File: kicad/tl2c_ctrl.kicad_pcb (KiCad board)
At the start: 4 copper layers, 38.1 x 66 mm, 65 parts, among them IC101 ATTINY20-X, P101 12VDC, P102 I2C Master, P103 Spare, P104 ISP Header, P105 LED_DRIVER, P301 PIR13, Q301 IRLML2502, Q302 IRLML2502, Q303 IRLML2502, SW101 TL3315NF160Q, U201 LF120ABDT-TR, U202 TPS70933

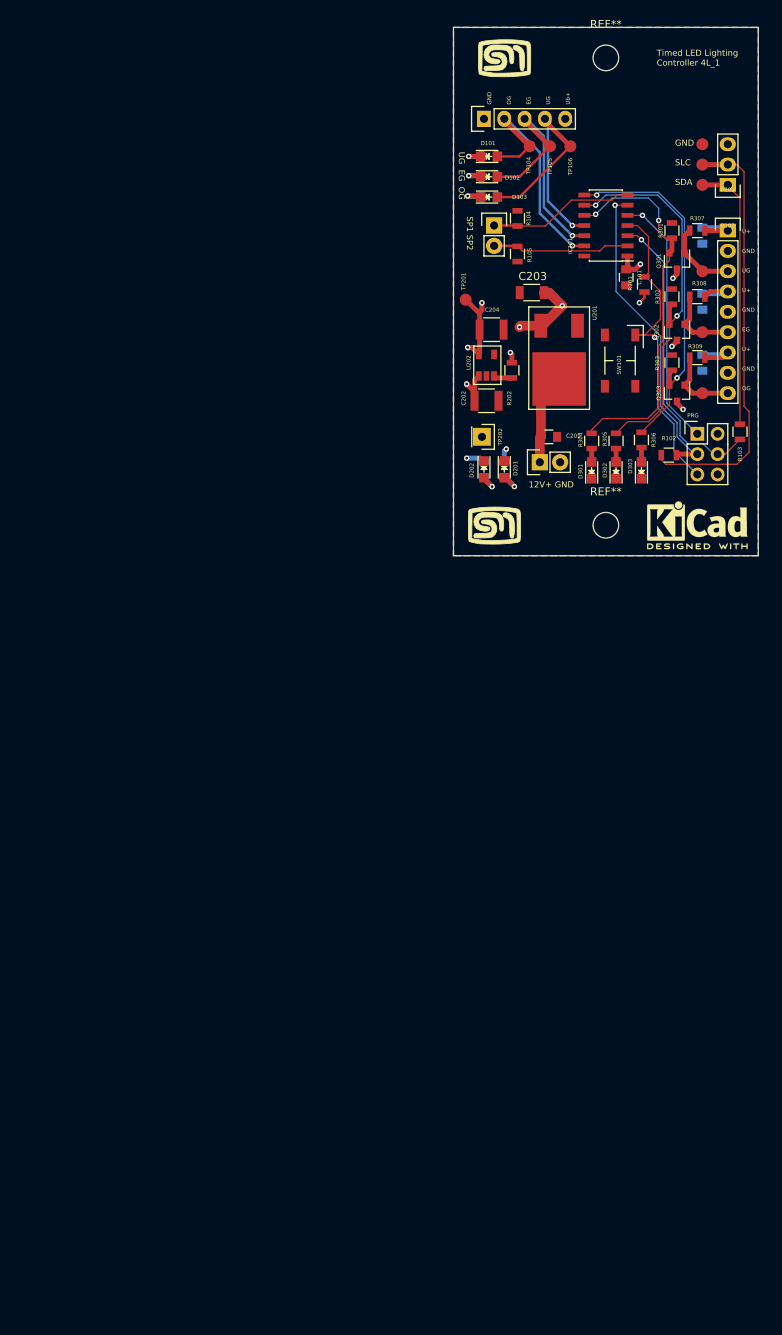
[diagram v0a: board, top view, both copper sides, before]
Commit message: Created the Gerbers and submitted the order for boards and stensils
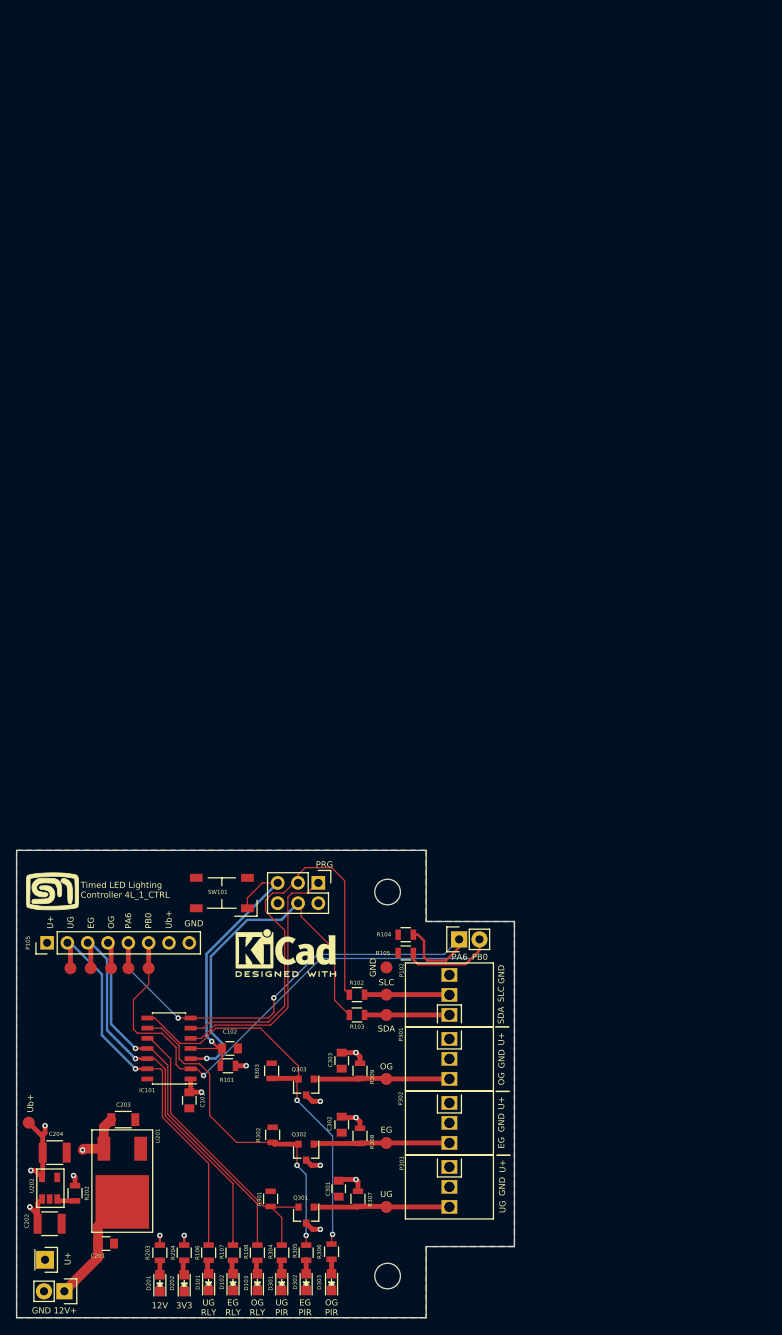
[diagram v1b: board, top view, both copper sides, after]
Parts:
- removed the G*** at (152.4, 80.0)
- removed the REF** at (166.4, 21.6)
- removed the REF** at (166.4, 80.0)
- added C102: 100n 50V, Capacitors_SMD:C_0805, F.Cu at (119.4, 145.4)
- added P302: CONN_PIR_EG, tl2c-footprint:Spring_Terminal_Block_1_x_3, F.Cu at (146.8, 152.2)
- added P303: CONN_PIR_UG, tl2c-footprint:Spring_Terminal_Block_1_x_3, F.Cu at (146.8, 160.2)
- added REF**: MountingHole_3.2mm_M3, Mounting_Holes:MountingHole_3.2mm_M3, F.Cu at (139.1, 125.9)
- added REF**: MountingHole_3.2mm_M3, Mounting_Holes:MountingHole_3.2mm_M3, F.Cu at (139.1, 173.9)
- added TP107: PA6, Measurement_Points:Measurement_Point_Round-SMD-Pad_Small, F.Cu at (106.7, 135.4)
- added TP108: PB0, Measurement_Points:Measurement_Point_Round-SMD-Pad_Small, F.Cu at (109.2, 135.4)
- C101: value 100n 10V -> 100n 50V
- C301, C302, C303, R106, R107, R108, R203, R204: moved to F.Cu
- P102: footprint Pin_Headers:Pin_Header_Straight_1x03 -> tl2c-footprint:Spring_Terminal_Block_1_x_3
- P105: footprint Pin_Headers:Pin_Header_Straight_1x05 -> Pin_Headers:Pin_Header_Straight_1x08_Pitch2.54mm
- P301: value PIR13 -> CONN_PIR_OG; footprint Pin_Headers:Pin_Header_Straight_1x09 -> tl2c-footprint:Spring_Terminal_Block_1_x_3
- moved D101 145.0 mm to (116.7, 174.6), turned to 90 degrees
- moved D102 141.8 mm to (119.8, 174.6), turned to 90 degrees
- moved R106 141.4 mm to (116.7, 170.9), turned to 270 degrees
- moved D103 138.7 mm to (122.8, 174.6), turned to 90 degrees
- moved R107 138.2 mm to (119.8, 170.9), turned to 270 degrees
- moved R108 135.1 mm to (122.8, 170.9), turned to 270 degrees
- moved R301 131.0 mm to (124.5, 164.2)
- moved R307 128.2 mm to (135.4, 164.2), turned to 90 degrees
- moved Q301 127.9 mm to (128.9, 166.2)
- moved C301 127.5 mm to (133.0, 162.9)
- moved TP301 123.5 mm to (138.9, 165.2)
- moved P101 119.5 mm to (98.7, 175.8), turned to 270 degrees
- moved G*** 118.5 mm to (97.2, 125.7)
- moved TP104 117.7 mm to (99.4, 135.4)
- moved TP105 117.7 mm to (102.0, 135.4)
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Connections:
- net /Reset renamed /~Reset
- D101 pad 1: Net-(D101-Pad1) -> GND
- D101 pad 2: /RelayUG -> Net-(D101-Pad2)
- D102 pad 1: Net-(D102-Pad1) -> GND
- D102 pad 2: /RelayEG -> Net-(D102-Pad2)
- D103 pad 1: Net-(D103-Pad1) -> GND
- D103 pad 2: /RelayOG -> Net-(D103-Pad2)
- IC101 pad 2: /Spare2 -> /GPIO_PB0
- IC101 pad 7: /Spare1 -> /GPIO_PA6
- P103 pad 1: /Spare1 -> /GPIO_PA6
- P103 pad 2: /Spare2 -> /GPIO_PB0
- P105 pad 1: /PIR13/Ub+ -> /PIR13/U+
- P105 pad 5: GND -> /GPIO_PA6
- P301 pad 3: /PIR13/PIR_UG -> /PIR13/PIR_OG
- R104 pad 2: /Spare1 -> /GPIO_PA6
- R105 pad 2: /Spare2 -> /GPIO_PB0
- R106 pad 1: Net-(D101-Pad1) -> /RelayUG
- R106 pad 2: GND -> Net-(D101-Pad2)
- R107 pad 1: Net-(D102-Pad1) -> /RelayEG
- R107 pad 2: GND -> Net-(D102-Pad2)
- R108 pad 1: Net-(D103-Pad1) -> /RelayOG
- R108 pad 2: GND -> Net-(D103-Pad2)
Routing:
- net /GPIO_PB0: track 0.00 -> 79.2 mm, vias 0 -> 1
- net /GPIO_PA6: track 0.00 -> 66.4 mm, vias 0 -> 2
- net /SCL: track 53.5 -> 10.6 mm
- net /SDA: track 33.7 -> 10.6 mm
- net /RelayUG: track 29.6 -> 50.5 mm
- net /RelayEG: track 30.9 -> 50.2 mm
- net /Spare1: track 18.6 -> 0.00 mm
- net /RelayOG: track 32.2 -> 50.2 mm
- net /Spare2: track 17.2 -> 0.00 mm
- net /SCK: track 40.6 -> 54.5 mm, vias 1 -> 0
- net /PIR13/U+: track 37.7 -> 26.1 mm, vias 5 -> 7
- net /MOSI: track 37.7 -> 47.7 mm
- net /PIR13/SIG_UG: track 48.1 -> 38.1 mm, vias 2 -> 0
- net /PIR13/PIR_UG: track 9.44 -> 17.2 mm
- net /PIR13/PIR_OG: track 9.52 -> 17.0 mm
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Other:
- board size 38.1 x 66 mm -> 62.2 x 58.4 mm
- rule pad_to_mask_clearance: 0.2 -> 0
- board text added: "12V"
- board text added: "3V3"
- board text added: "EG"
- board text added: "EG PIR"
- board text added: "EG RLY"
- board text added: "GND"
- board text added: "GND 12V+"
- board text added: "OG"
- board text added: "OG PIR"
- board text added: "OG RLY"
- board text added: "PA6"
- board text added: "PB0"
- board text added: "SDA"
- board text added: "SLC"
- board text added: "Timed LED Lighting Controller 4L_1_CTRL"
- board text added: "U+"
- board text added: "UG"
- board text added: "UG PIR"
- board text added: "UG RLY"
- board text added: "Ub+"
- board text removed: "12V+ GND"
- board text removed: "GND OG EG UG Ub+"
- board text removed: "GND SLC SDA"
- board text removed: "SP1 SP2"
- board text removed: "Timed LED Lighting Controller 4L_1"
- board text removed: "U+ GND UG U+ GND EG U+ GND OG"
- board text removed: "UG EG OG"

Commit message: Finalised the corrections to the board
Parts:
- removed R102: 330Ω, Resistors_SMD:R_0805
- added D203: 5VDC, LEDs:LED_0805, F.Cu at (107.7, 174.8)
- added P109: 5VDC, Pin_Headers:Pin_Header_Straight_1x02_Pitch2.54mm, F.Cu at (95.5, 146.1)
- added P201: Mode_Bridge, Pin_Headers:Pin_Header_Straight_1x03_Pitch2.54mm, F.Cu at (100.8, 143.6)
- added R201: 660Ω, Resistors_SMD:R_0805, F.Cu at (107.7, 170.9)
- C204: value 1μF 16V -> 2.2μF 16V
- P104: value ISP Header -> TPI Header; footprint Pin_Headers:Pin_Header_Straight_2x03 -> tl2c-footprint:TC2030-IDC-FP_ISP_Connector
- R103: value 330Ω -> 0Ω
- moved C203 10.4 mm to (111.8, 163.0), turned to 90 degrees
- moved U201 8.33 mm to (106.5, 156.3), turned to 270 degrees
- moved P104 4.01 mm to (126.5, 125.5), turned to 180 degrees
- moved C201 3.24 mm to (105.3, 166.9)
- moved TP101 1.15 mm to (137.8, 135.4)
- moved SW101 0.89 mm to (117.5, 126.0)
- moved TP201 0.51 mm to (94.7, 154.7)
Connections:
- C204 pad 1: /PIR13/Ub+ -> Net-(C204-Pad1)
- IC101 pad 2: /GPIO_PB0 -> /TPICLK
- IC101 pad 3: /MOSI -> /TPIDATA
- IC101 pad 5: /MISO -> /GPIO_PB2
- IC101 pad 6: /SCK -> /SCL
- P103 pad 2: /GPIO_PB0 -> /GPIO_PB2
- P104 pad 1: /MISO -> /TPIDATA
- P104 pad 3: /SCK -> /TPICLK
- P104 pad 4: /MOSI -> Net-(P104-Pad4)
- P105 pad 6: /GPIO_PB0 -> /GPIO_PB2
- R103 pad 2: /MOSI -> /TPIDATA
- R105 pad 2: /GPIO_PB0 -> /GPIO_PB2
- R204 pad 1: /PIR13/Ub+ -> Net-(C204-Pad1)
- TP108 pad 1: /GPIO_PB0 -> /GPIO_PB2
- TP201 pad 1: /PIR13/Ub+ -> Net-(C204-Pad1)
- U202 pad 5: /PIR13/Ub+ -> Net-(C204-Pad1)
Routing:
- net /GPIO_PB0: track 79.2 -> 0.00 mm, vias 1 -> 0
- net /GPIO_PB2: track 0.00 -> 65.4 mm, vias 0 -> 1
- net /SCK: track 54.5 -> 0.00 mm
- net Net-(C204-Pad1): track 0.00 -> 52.2 mm, vias 0 -> 3
- net /MOSI: track 47.7 -> 0.00 mm, vias 1 -> 0
- net /TPIDATA: track 0.00 -> 45.8 mm, vias 0 -> 3
- net /TPICLK: track 0.00 -> 40.9 mm, vias 0 -> 2
- net /Power System/5V: track 0.00 -> 35.7 mm, vias 0 -> 1
- net /MISO: track 32.1 -> 0.00 mm
- net /SCL: track 10.6 -> 34.1 mm
- net /PIR13/Ub+: track 23.0 -> 14.5 mm, vias 8 -> 6
- net /~Reset: track 37.4 -> 34.3 mm, vias 1 -> 2
- net /PIR13/U+: track 26.1 -> 29.0 mm, vias 7 -> 8
- net GND: track 0.00 -> 2.36 mm, vias 0 -> 1
- net /Power System/U+In: track 17.4 -> 15.2 mm
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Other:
- board text added: "*"
- board text added: "5V ISP"
- board text added: "PRG 5V"
- board text added: "RUN PRG"
- board text added: "Timed LED Lighting Controller 4L_2_CTRL Control Board"
- board text removed: "Timed LED Lighting Controller 4L_1_CTRL"
